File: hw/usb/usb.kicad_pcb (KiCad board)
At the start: 6 copper layers, 100 x 100 mm, 260 parts, among them J1 USB3_MICRO_AB, J2 USB3_MICRO_AB, J3 BARREL_JACK, J4 SAMTEC_QSH-090-D, P4 CONN_1, P5 CONN_1, P6 CONN_1, P7 CONN_1, P8 CONN_1, Q1 MOSFET_P, Q2 MOSFET_P, U1 TUSB1310A, U10 TPS62420, U11 TPS54821, U12 ON_CAT24C256, U13 TCA6416ARTW, U14 TCA6416ARTW, U2 TPS2065C-2, U3 GSG-IP4220CZ6, U4 USB3_ESD_SON50-10, U5 TUSB1310A, U6 TPS2065C-2, U7 GSG-IP4220CZ6, U8 USB3_ESD_SON50-10, U9 MIC5207YM5, X1 40M, X2 40M

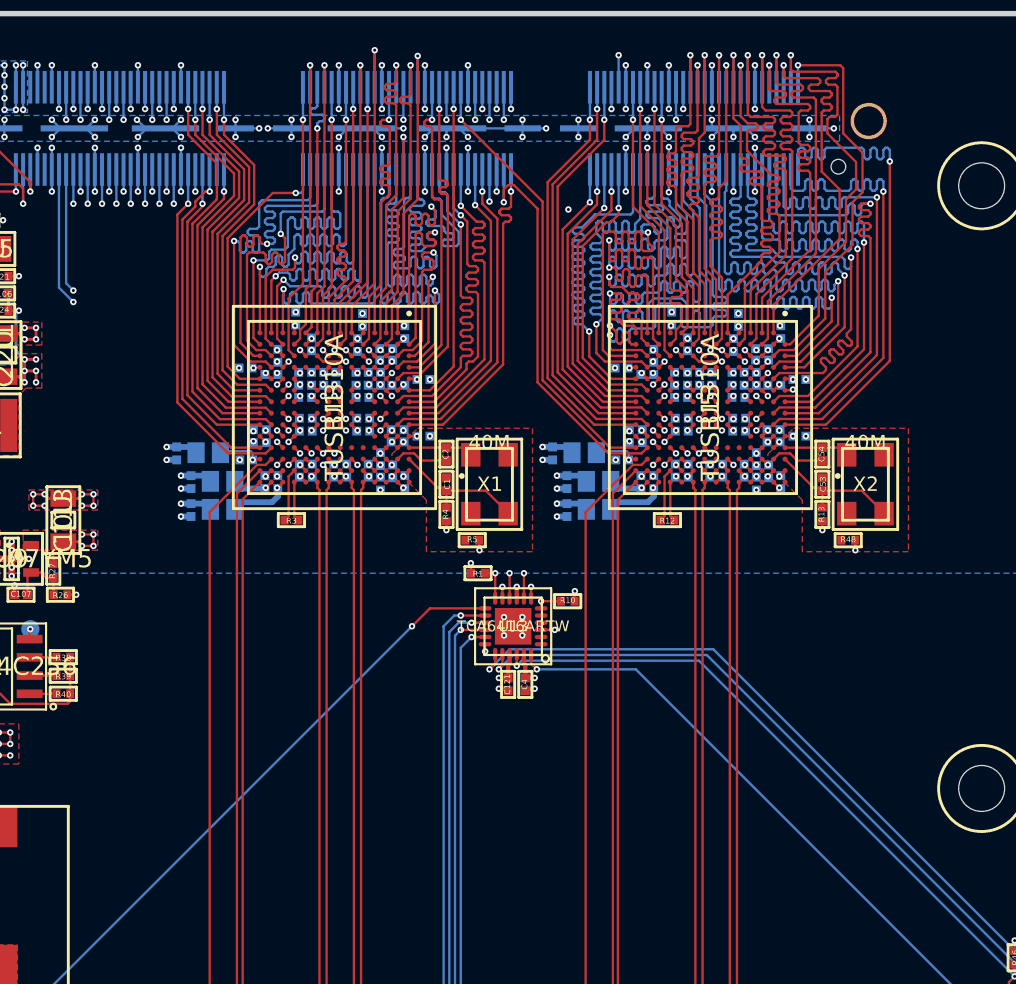
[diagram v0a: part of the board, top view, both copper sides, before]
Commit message: PCB: Delete extra nets/traces, fix DRC errors, add "do not manufacture" silkscreen.
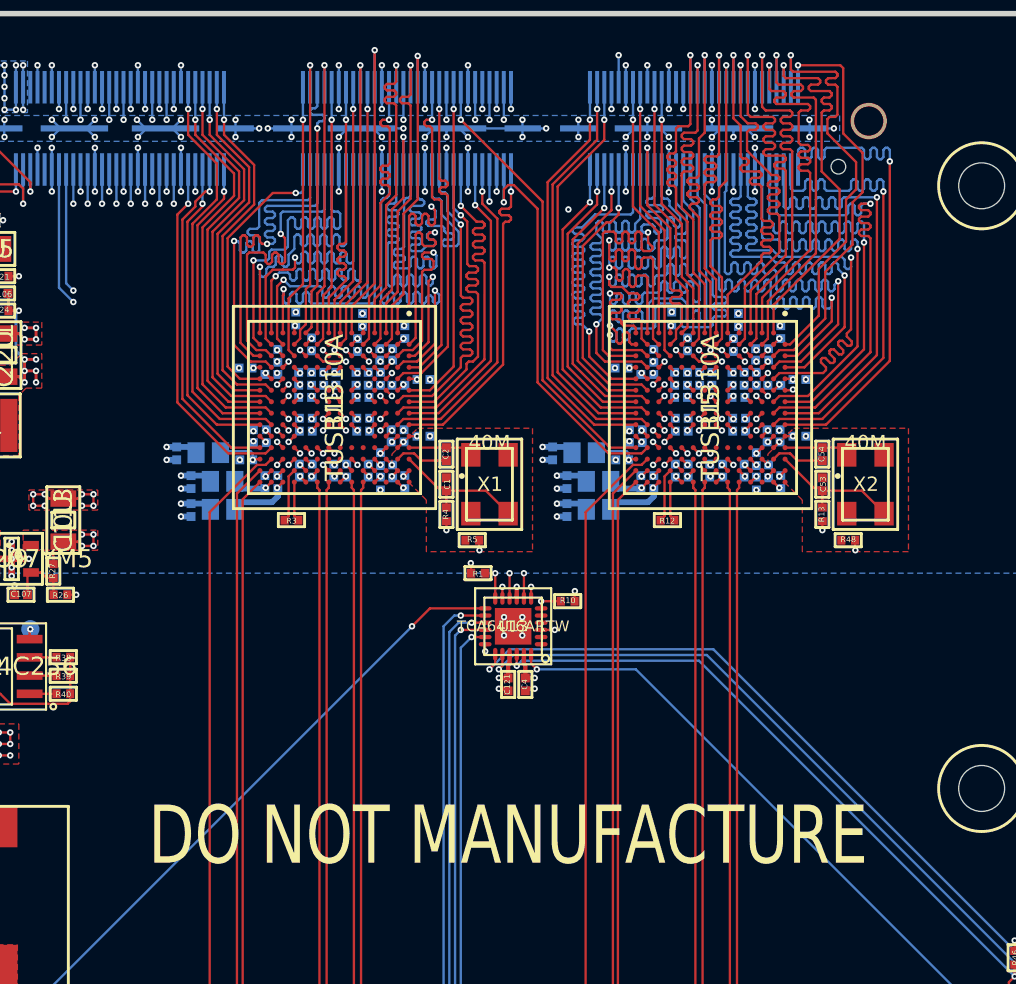
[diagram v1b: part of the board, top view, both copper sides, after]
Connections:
- J3 pad 3: Net-(J3-Pad3) -> (no net)
- J4 pad 10: /main_board_if/FE_CLK_N0 -> (no net)
- J4 pad 145: Net-(J4-Pad145) -> (no net)
- J4 pad 5: /main_board_if/FE_CLKSRC -> (no net)
- J4 pad 58: Net-(J4-Pad58) -> (no net)
- J4 pad 9: /main_board_if/FE_CLK_N1 -> (no net)
- U1 pad A14: Net-(U1-PadA14) -> (no net)
- U1 pad C13: Net-(U1-PadC13) -> (no net)
- U1 pad C14: Net-(U1-PadC14) -> (no net)
- U1 pad D10: Net-(U1-PadD10) -> (no net)
- U1 pad D11: Net-(U1-PadD11) -> (no net)
- U1 pad D5: Net-(U1-PadD5) -> (no net)
- U1 pad D6: Net-(U1-PadD6) -> (no net)
- U1 pad E11: Net-(U1-PadE11) -> (no net)
- U1 pad E12: Net-(U1-PadE12) -> (no net)
- U1 pad F11: Net-(U1-PadF11) -> (no net)
- U1 pad G11: Net-(U1-PadG11) -> (no net)
- U1 pad H12: Net-(U1-PadH12) -> (no net)
- U1 pad J12: Net-(U1-PadJ12) -> (no net)
- U1 pad J4: Net-(U1-PadJ4) -> (no net)
- U1 pad K4: Net-(U1-PadK4) -> (no net)
- U1 pad L6: Net-(U1-PadL6) -> (no net)
- U13 pad 1: Net-(U13-Pad1) -> (no net)
- U13 pad 2: Net-(U13-Pad2) -> (no net)
- U13 pad 4: Net-(U13-Pad4) -> (no net)
- U13 pad 5: Net-(U13-Pad5) -> (no net)
- U3 pad 6: Net-(U3-Pad6) -> (no net)
- U5 pad A14: Net-(U5-PadA14) -> (no net)
- U5 pad C13: Net-(U5-PadC13) -> (no net)
- U5 pad C14: Net-(U5-PadC14) -> (no net)
- U5 pad D10: Net-(U5-PadD10) -> (no net)
- U5 pad D11: Net-(U5-PadD11) -> (no net)
- U5 pad D5: Net-(U5-PadD5) -> (no net)
- U5 pad D6: Net-(U5-PadD6) -> (no net)
- U5 pad E11: Net-(U5-PadE11) -> (no net)
- U5 pad E12: Net-(U5-PadE12) -> (no net)
- U5 pad F11: Net-(U5-PadF11) -> (no net)
- U5 pad G11: Net-(U5-PadG11) -> (no net)
- U5 pad H12: Net-(U5-PadH12) -> (no net)
- U5 pad J12: Net-(U5-PadJ12) -> (no net)
- U5 pad J4: Net-(U5-PadJ4) -> (no net)
- U5 pad K4: Net-(U5-PadK4) -> (no net)
- U5 pad L6: Net-(U5-PadL6) -> (no net)
- U7 pad 6: Net-(U7-Pad6) -> (no net)
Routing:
- net Net-(J4-Pad145): track 2.27 -> 0.00 mm, vias 1 -> 0
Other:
- board text added: "DO NOT MANUFACTURE"

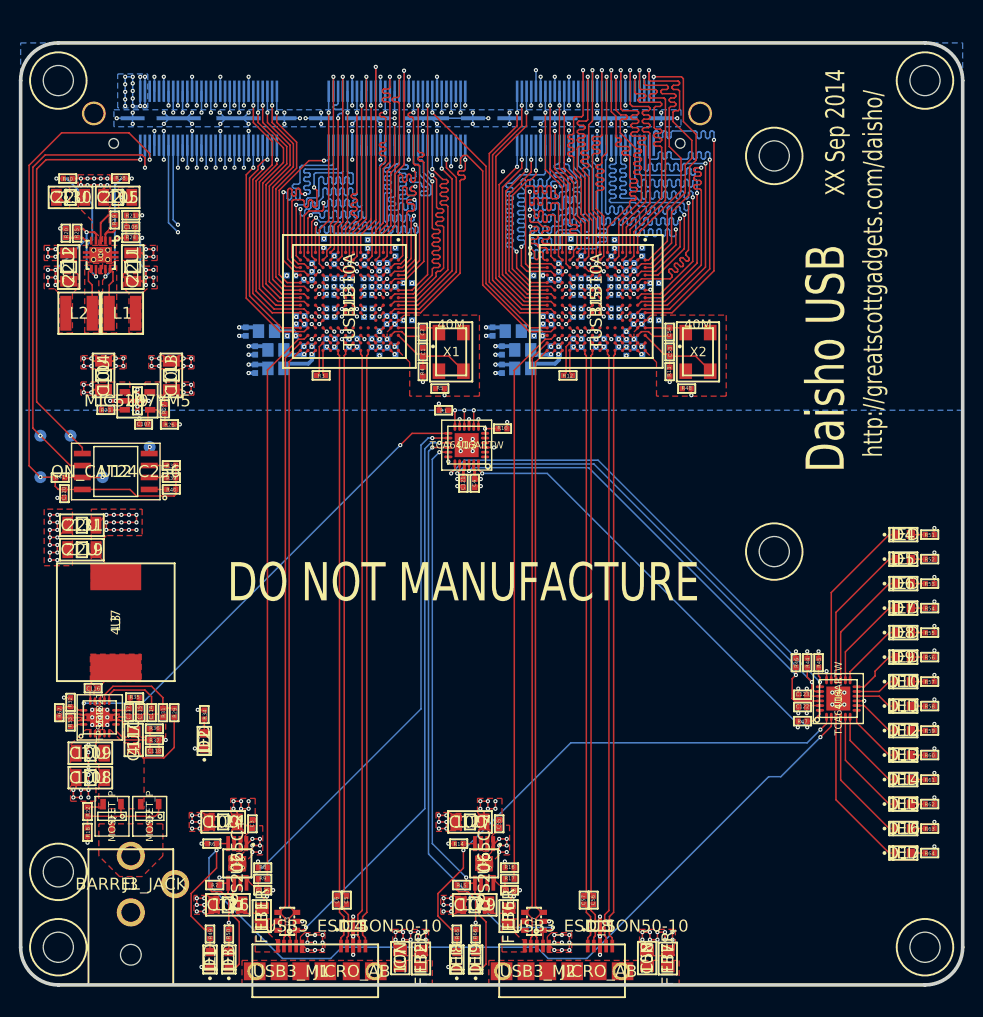
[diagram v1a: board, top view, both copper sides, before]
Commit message: USB: Update PCB with schematic changes, controlled impedance net class and trace widths.
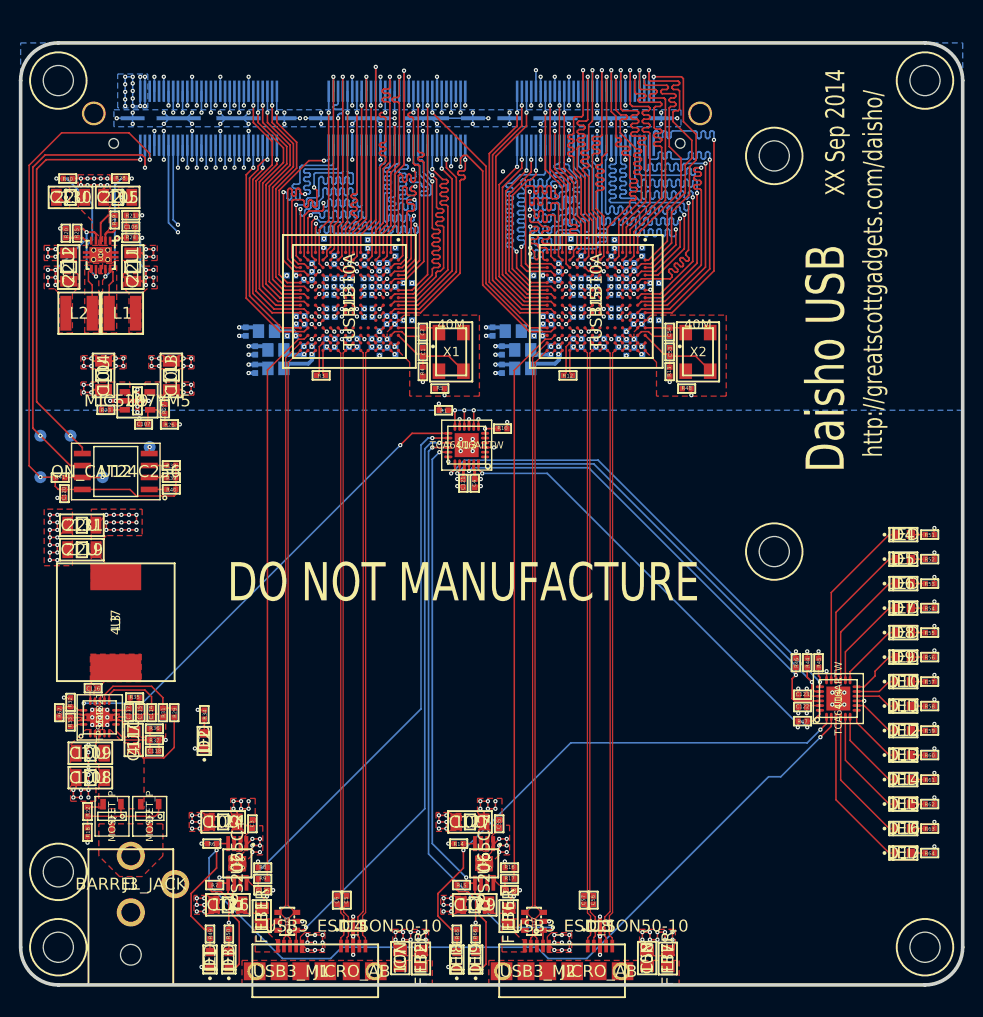
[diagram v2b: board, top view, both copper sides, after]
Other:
- net class 50_se added: clearance 0.127, trace_width 0.1651, via_dia 0.4572, via_drill 0.2032
- net class 90_diff added: clearance 0.127, trace_width 0.127, via_dia 0.4572, via_drill 0.2032
- net class Default: via_dia 0.44958 -> 0.4572
- rule solder_mask_min_width: 0.1016 -> 0.0762
- rule trace_min: 0.1651 -> 0.127
- rule via_min_size: 0.44958 -> 0.4572

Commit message: PCB: Final clean-up
HSMC grounding tweaks.
Connect a ground island (still served by other ground plane, but...).
Add clearance to some copper pours.
Remove "DO NOT MANUFACTURE".
Update PCB date code.
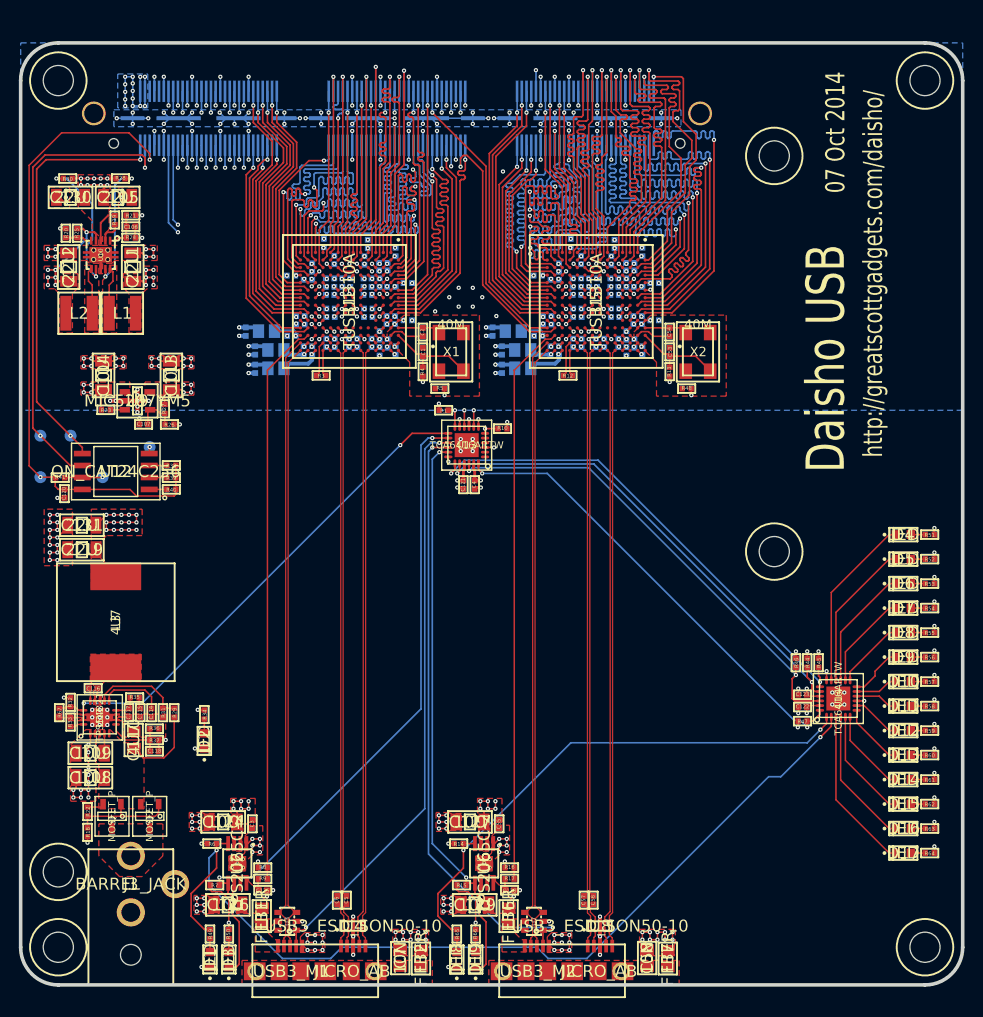
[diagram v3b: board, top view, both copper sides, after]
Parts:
- moved C121 0.15 mm to (124.5, 95.4)
- moved C4 0.15 mm to (125.7, 95.4)
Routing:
- net GND: track 260.6 -> 291.5 mm, vias 343 -> 356
- net V1P8: track 106.0 -> 102.6 mm
- net /main_board_if/USB0_XI: track 134.0 -> 131.4 mm
- net /power/SW_PVIN: track 10.2 -> 12.8 mm
- net /power/SW_PH: track 0.00 -> 2.36 mm
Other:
- board text added: "07 Oct 2014"
- board text removed: "DO NOT MANUFACTURE"
- board text removed: "XX Sep 2014"
